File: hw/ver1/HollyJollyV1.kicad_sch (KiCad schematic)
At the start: 34 parts, among them J1 USB_B_Micro, Q1 2N7002, SW1 BOOT, SW2 CYCLE, U1 RP2040, U2 W25Q128JVS, U3 XC6206PxxxMR, Y1 12MHz

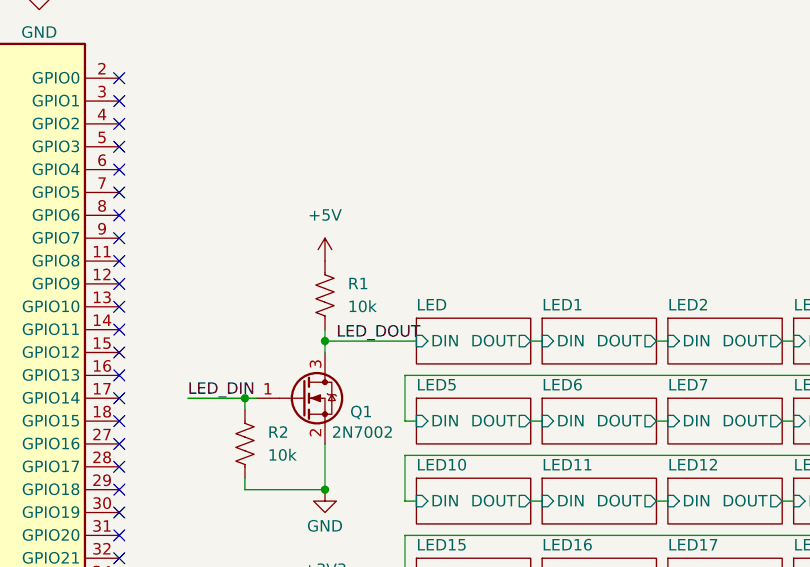
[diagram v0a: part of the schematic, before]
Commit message: Nearly have all the LEDs wired up. Improve the christmas cheer.
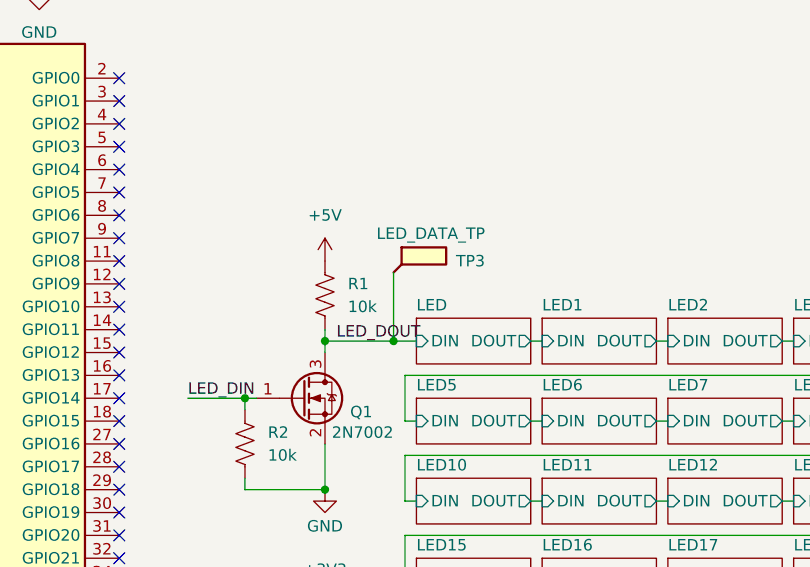
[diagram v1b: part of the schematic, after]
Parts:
- added TP3: LED_DATA_TP, TestPoint:TestPoint_Pad_1.0x1.0mm, symbol Connector:TestPoint_Flag
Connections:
- net LED_DOUT: now also TP3.1
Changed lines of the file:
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@@
 	)
 	(junction
+		(at 205.74 81.28)
+		(diameter 0)
+		(color 0 0 0 0)
+	)
+	(junction
 		(at 118.11 107.95)
 		(diameter 0)
@@
 	(wire
 		(pts
+			(xy 205.74 81.28) (xy 208.28 81.28)
+		)
+		(stroke
+			(width 0)
+			(type default)
+		)
+	)
+	(wire
+		(pts
 			(xy 220.98 107.95) (xy 222.25 107.95)
 		)
@@
 	(wire
 		(pts
-			(xy 198.12 81.28) (xy 208.28 81.28)
+			(xy 198.12 81.28) (xy 205.74 81.28)
 		)
 		(stroke
@@
 	(wire
 		(pts
+			(xy 205.74 73.66) (xy 205.74 81.28)
+		)
+		(stroke
+			(width 0)
+			(type default)
+		)
+	)
+	(wire
+		(pts
 			(xy 134.62 29.21) (xy 134.62 30.48)
 		)
@@
 					(unit 1)
 				)
+			)
+		)
+	)
+	(symbol
+		(lib_id "Connector:TestPoint_Flag")
+		(at 205.74 73.66 0)
+		(unit 1)
+		(exclude_from_sim no)
+		(in_bom yes)
+		(on_board yes)
+		(dnp no)
+		(property "Reference" "TP3"
+			(at 215.9 72.39 0)
+			(effects
+				(font
+					(size 1.27 1.27)
+				)
+				(justify right)
+			)
+		)
+		(property "Value" "LED_DATA_TP"
+			(at 215.9 69.342 0)
+			(effects
+				(font
+					(size 1.27 1.27)
+				)
+				(justify right)
+			)
+		)
+		(property "Footprint" "TestPoint:TestPoint_Pad_1.0x1.0mm"
+			(at 210.82 73.66 0)
+			(effects
+				(font
+					(size 1.27 1.27)
+				)
+				(hide yes)
+			)
+		)
+		(property "Datasheet" "~"
+			(at 210.82 73.66 0)
+			(effects
+				(font
+					(size 1.27 1.27)
+				)
+				(hide yes)
+			)
+		)
+		(property "Description" "test point (alternative flag-style design)"
+			(at 205.74 73.66 0)
+			(effects
+				(font
+					(size 1.27 1.27)
+				)
+				(hide yes)
+			)
+		)
+		(pin "1"
+		)
+		(instances
+			(project "HollyJollyV1"
+				(path "/6b41699c-714d-4006-8719-4b1ad5a2d228"
+					(reference "TP3")
+					(unit 1)
+				)

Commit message: Hardware version 1 complete and ordered.
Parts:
- added C43: 100nF, Capacitor_SMD:C_0402_1005Metric, symbol Device:C
- added R8: 10k, Resistor_SMD:R_0402_1005Metric, symbol Device:R_US
- added SW3: BRIGHT, Button_Switch_SMD:SW_Push_SPST_NO_Alps_SKRK, symbol Switch:SW_Push
- J1: JLCPCB Position Offset (none) -> 0,2.5; JLCPCB Rotation Offset (none) -> -180
- U1: JLCPCB Rotation Offset (none) -> -90
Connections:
- net +3V3: now also R8.2
- net GND: now also C43.2, SW3.1
- net LED_BRIGHT: now reaches U1.30 (GPIO19)
- net LED_BRIGHT: now also C43.1, R8.1, SW3.2
- no-connect marks 30 -> 29
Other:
- added sheet LED25 (ws2812.kicad_sch)
- added sheet LED26 (ws2812.kicad_sch)
- added sheet LED27 (ws2812.kicad_sch)
- added sheet LED28 (ws2812.kicad_sch)
- added sheet LED29 (ws2812.kicad_sch)
- added sheet LED30 (ws2812.kicad_sch)
- added sheet LED31 (ws2812.kicad_sch)
- moved on the sheet: C1, C10, C11, C12, C13, C14, C15, C16, C17, C2, C3, C4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
